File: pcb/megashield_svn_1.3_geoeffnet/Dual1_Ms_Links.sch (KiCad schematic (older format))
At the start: 7 parts, among them P18 Left

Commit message: Platine V1.3
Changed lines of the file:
@@
 LIBS:power
 LIBS:ardumower mega shield svn-cache
+LIBS:conn
 EELAYER 25 0
 EELAYER END
@@
 P 4895 3310
 AR Path="/553D8AD9/5542A35A/554BE910" Ref="#PWR0137"  Part="1"
-AR Path="/553D8AD9/554D3EE8/554BE910" Ref="#PWR0143"  Part="1"
-F 0 "#PWR0143" H 4895 3160 60  0001 C CNN
+AR Path="/553D8AD9/554D3EE8/554BE910" Ref="#PWR0145"  Part="1"
+F 0 "#PWR0145" H 4895 3160 60  0001 C CNN
 F 1 "+24V" H 4895 3450 60  0000 C CNN
 F 2 "" H 4895 3310 60  0000 C CNN
@@
 P 4895 4445
 AR Path="/553D8AD9/5542A35A/5542A3C5" Ref="#PWR0138"  Part="1"
-AR Path="/553D8AD9/554D3EE8/5542A3C5" Ref="#PWR0144"  Part="1"
-F 0 "#PWR0144" H 4895 4195 60  0001 C CNN
+AR Path="/553D8AD9/554D3EE8/5542A3C5" Ref="#PWR0146"  Part="1"
+F 0 "#PWR0146" H 4895 4195 60  0001 C CNN
 F 1 "GND" H 4895 4295 60  0000 C CNN
 F 2 "" H 4895 4445 60  0000 C CNN
@@
 P 4895 3580
 AR Path="/553D8AD9/5542A35A/5542A3D9" Ref="BY3"  Part="1"
-AR Path="/553D8AD9/554D3EE8/5542A3D9" Ref="BY7"  Part="1"
-F 0 "BY7" H 4895 3680 40  0000 C CNN
+AR Path="/553D8AD9/554D3EE8/5542A3D9" Ref="DBY7"  Part="1"
+F 0 "DBY7" H 4895 3680 40  0000 C CNN
 F 1 "BY 500/1000" H 4895 3480 40  0000 C CNN
 F 2 "ACS712:Diode_liegend_BY500_1000_RM10" H 4895 3580 60  0001 C CNN
@@
 P 4895 4140
 AR Path="/553D8AD9/5542A35A/5542A4FC" Ref="BY4"  Part="1"
-AR Path="/553D8AD9/554D3EE8/5542A4FC" Ref="BY8"  Part="1"
-F 0 "BY8" H 4895 4240 40  0000 C CNN
+AR Path="/553D8AD9/554D3EE8/5542A4FC" Ref="DBY8"  Part="1"
+F 0 "DBY8" H 4895 4240 40  0000 C CNN
 F 1 "BY 500/1000" H 4895 4040 40  0000 C CNN
 F 2 "ACS712:Diode_liegend_BY500_1000_RM10" H 4895 4140 60  0001 C CNN
@@
 P 3170 3310
 AR Path="/553D8AD9/5542A35A/5542A69A" Ref="#PWR0139"  Part="1"
-AR Path="/553D8AD9/554D3EE8/5542A69A" Ref="#PWR0145"  Part="1"
-F 0 "#PWR0145" H 3170 3160 60  0001 C CNN
+AR Path="/553D8AD9/554D3EE8/5542A69A" Ref="#PWR0147"  Part="1"
+F 0 "#PWR0147" H 3170 3160 60  0001 C CNN
 F 1 "+24V" H 3170 3450 60  0000 C CNN
 F 2 "" H 3170 3310 60  0000 C CNN
@@
 P 3170 4445
 AR Path="/553D8AD9/5542A35A/554BE919" Ref="#PWR0140"  Part="1"
-AR Path="/553D8AD9/554D3EE8/554BE919" Ref="#PWR0146"  Part="1"
-F 0 "#PWR0146" H 3170 4195 60  0001 C CNN
+AR Path="/553D8AD9/554D3EE8/554BE919" Ref="#PWR0148"  Part="1"
+F 0 "#PWR0148" H 3170 4195 60  0001 C CNN
 F 1 "GND" H 3170 4295 60  0000 C CNN
 F 2 "" H 3170 4445 60  0000 C CNN
@@
 P 3170 3580
 AR Path="/553D8AD9/5542A35A/554BE91B" Ref="BY1"  Part="1"
-AR Path="/553D8AD9/554D3EE8/554BE91B" Ref="BY5"  Part="1"
-F 0 "BY5" H 3170 3680 40  0000 C CNN
+AR Path="/553D8AD9/554D3EE8/554BE91B" Ref="DBY5"  Part="1"
+F 0 "DBY5" H 3170 3680 40  0000 C CNN
 F 1 "BY 500/1000" H 3170 3480 40  0000 C CNN
 F 2 "ACS712:Diode_liegend_BY500_1000_RM10" H 3170 3580 60  0001 C CNN
@@
 P 3170 4140
 AR Path="/553D8AD9/5542A35A/554BE91D" Ref="BY2"  Part="1"
-AR Path="/553D8AD9/554D3EE8/554BE91D" Ref="BY6"  Part="1"
-F 0 "BY6" H 3170 4240 40  0000 C CNN
+AR Path="/553D8AD9/554D3EE8/554BE91D" Ref="DBY6"  Part="1"
+F 0 "DBY6" H 3170 4240 40  0000 C CNN
 F 1 "BY 500/1000" H 3170 4040 40  0000 C CNN
 F 2 "ACS712:Diode_liegend_BY500_1000_RM10" H 3170 4140 60  0001 C CNN

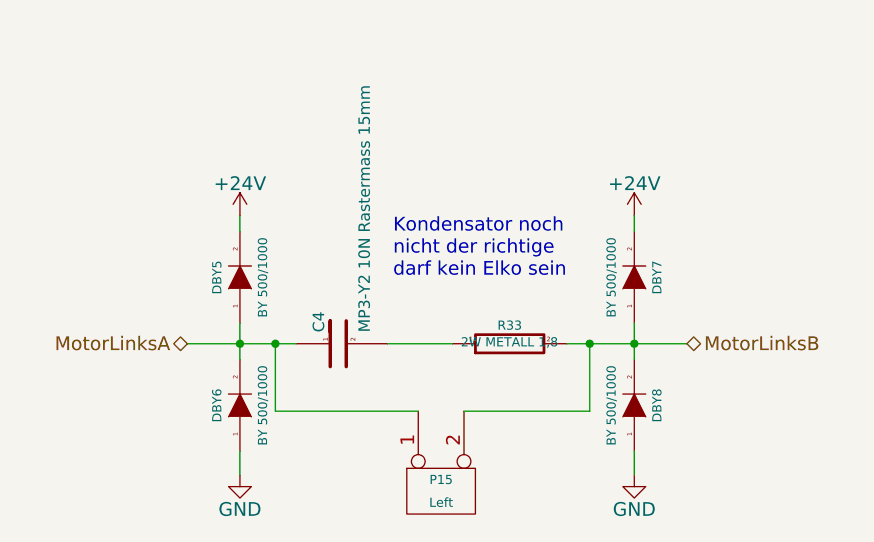
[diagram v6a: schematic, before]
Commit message: Platine V1.3
Einzelne Bauteile auf SMD angepasst
Belegung Anschlussstecker geändert +5V und GND
Anschlussstecker auf KK Stecker umgeändert
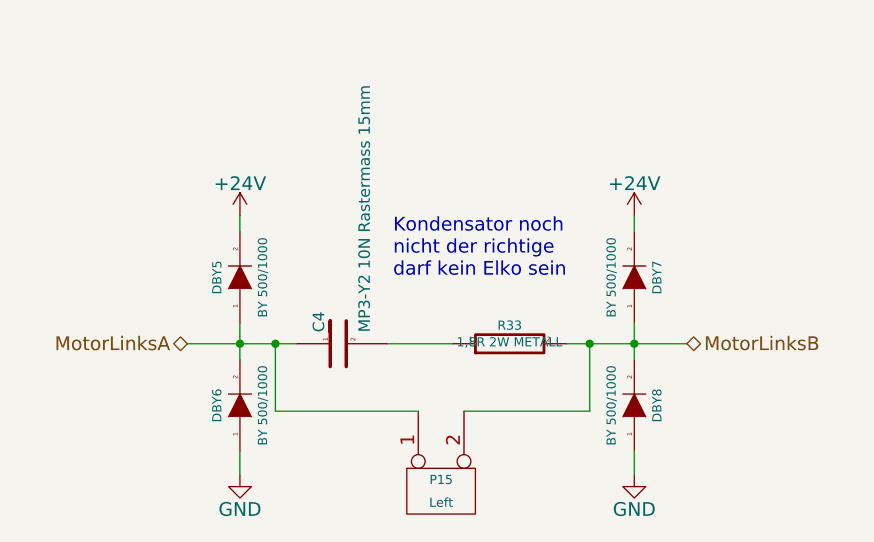
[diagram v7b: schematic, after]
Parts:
- BY1, BY2, BY3, BY4: footprint ACS712:Diode_liegend_BY500_1000_RM10 -> Diodes_ThroughHole:Diode_DO-201AD_Horizontal_RM15; Bauform (none) -> DO-201; Bestelllink (none) -> https://www.reichelt.de/BY-500-1000/3/index.html?&ACTION=3&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
- R33: value 2W METALL 1,8 -> 1,8R 2W METALL; footprint ACS712:Resistor_Horizontal_RM20mm -> Resistors_SMD:R_2512
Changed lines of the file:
@@
 $Descr A4 11693 8268
 encoding utf-8
-Sheet 15 27
+Sheet 15 25
 Title "Ardumower Shield - Motortreiber 1 - Links"
 Date ""
@@
 P 4895 3310
 AR Path="/553D8AD9/5542A35A/554BE910" Ref="#PWR0137"  Part="1"
-AR Path="/553D8AD9/554D3EE8/554BE910" Ref="#PWR0149"  Part="1"
-F 0 "#PWR0149" H 4895 3160 60  0001 C CNN
+AR Path="/553D8AD9/554D3EE8/554BE910" Ref="#PWR0159"  Part="1"
+F 0 "#PWR0159" H 4895 3160 60  0001 C CNN
 F 1 "+24V" H 4895 3450 60  0000 C CNN
 F 2 "" H 4895 3310 60  0000 C CNN
@@
 P 4895 4445
 AR Path="/553D8AD9/5542A35A/5542A3C5" Ref="#PWR0138"  Part="1"
-AR Path="/553D8AD9/554D3EE8/5542A3C5" Ref="#PWR0150"  Part="1"
-F 0 "#PWR0150" H 4895 4195 60  0001 C CNN
+AR Path="/553D8AD9/554D3EE8/5542A3C5" Ref="#PWR0160"  Part="1"
+F 0 "#PWR0160" H 4895 4195 60  0001 C CNN
 F 1 "GND" H 4895 4295 60  0000 C CNN
 F 2 "" H 4895 4445 60  0000 C CNN
@@
 F 0 "DBY7" H 4895 3680 40  0000 C CNN
 F 1 "BY 500/1000" H 4895 3480 40  0000 C CNN
-F 2 "ACS712:Diode_liegend_BY500_1000_RM10" H 4895 3580 60  0001 C CNN
+F 2 "Diodes_ThroughHole:Diode_DO-201AD_Horizontal_RM15" H 4895 3580 60  0001 C CNN
 F 3 "https://www.reichelt.de/BY-500-1000/3/index.html?&ACTION=3&LA=446&ARTICLE=6337&artnr=BY+500%2F1000&SEARCH=BY+500%2F1000" H 4895 3580 60  0001 C CNN
-F 4 "R: BY 500/1000" H 4895 3580 60  0001 C CNN "Bestellnummer"
-F 5 "Fast-Recovery-Gleichr.-Diode, DO201, 1000V, 5A" H 4895 3580 60  0001 C CNN "Technische Daten"
+F 4 "Fast-Recovery-Gleichr.-Diode, DO201, 1000V, 5A" H 4895 3580 60  0001 C CNN "Technische Daten"
+F 5 "R: BY 500/1000" H 4895 3580 60  0001 C CNN "Bestellnummer"
+F 6 "DO-201" H 4895 3580 60  0001 C CNN "Bauform"
+F 7 "https://www.reichelt.de/BY-500-1000/3/index.html?&ACTION=3&LA=446&ARTICLE=6337&artnr=BY+500%2F1000&SEARCH=BY+500%2F1000" H 4895 3580 60  0001 C CNN "Bestelllink"
 	1    4895 3580
 	0    1    -1   0
@@
 F 0 "DBY8" H 4895 4240 40  0000 C CNN
 F 1 "BY 500/1000" H 4895 4040 40  0000 C CNN
-F 2 "ACS712:Diode_liegend_BY500_1000_RM10" H 4895 4140 60  0001 C CNN
+F 2 "Diodes_ThroughHole:Diode_DO-201AD_Horizontal_RM15" H 4895 4140 60  0001 C CNN
 F 3 "https://www.reichelt.de/BY-500-1000/3/index.html?&ACTION=3&LA=446&ARTICLE=6337&artnr=BY+500%2F1000&SEARCH=BY+500%2F1000" H 4895 4140 60  0001 C CNN
-F 4 "R: BY 500/1000" H 4895 4140 60  0001 C CNN "Bestellnummer"
-F 5 "Fast-Recovery-Gleichr.-Diode, DO201, 1000V, 5A" H 4895 4140 60  0001 C CNN "Technische Daten"
+F 4 "Fast-Recovery-Gleichr.-Diode, DO201, 1000V, 5A" H 4895 4140 60  0001 C CNN "Technische Daten"
+F 5 "R: BY 500/1000" H 4895 4140 60  0001 C CNN "Bestellnummer"
+F 6 "DO-201" H 4895 4140 60  0001 C CNN "Bauform"
+F 7 "https://www.reichelt.de/BY-500-1000/3/index.html?&ACTION=3&LA=446&ARTICLE=6337&artnr=BY+500%2F1000&SEARCH=BY+500%2F1000" H 4895 4140 60  0001 C CNN "Bestelllink"
 	1    4895 4140
 	0    1    -1   0
@@
 P 3170 3310
 AR Path="/553D8AD9/5542A35A/5542A69A" Ref="#PWR0139"  Part="1"
-AR Path="/553D8AD9/554D3EE8/5542A69A" Ref="#PWR0151"  Part="1"
-F 0 "#PWR0151" H 3170 3160 60  0001 C CNN
+AR Path="/553D8AD9/554D3EE8/5542A69A" Ref="#PWR0161"  Part="1"
+F 0 "#PWR0161" H 3170 3160 60  0001 C CNN
 F 1 "+24V" H 3170 3450 60  0000 C CNN
 F 2 "" H 3170 3310 60  0000 C CNN
@@
 P 3170 4445
 AR Path="/553D8AD9/5542A35A/554BE919" Ref="#PWR0140"  Part="1"
-AR Path="/553D8AD9/554D3EE8/554BE919" Ref="#PWR0152"  Part="1"
-F 0 "#PWR0152" H 3170 4195 60  0001 C CNN
+AR Path="/553D8AD9/554D3EE8/554BE919" Ref="#PWR0162"  Part="1"
+F 0 "#PWR0162" H 3170 4195 60  0001 C CNN
 F 1 "GND" H 3170 4295 60  0000 C CNN
 F 2 "" H 3170 4445 60  0000 C CNN
@@
 F 0 "DBY5" H 3170 3680 40  0000 C CNN
 F 1 "BY 500/1000" H 3170 3480 40  0000 C CNN
-F 2 "ACS712:Diode_liegend_BY500_1000_RM10" H 3170 3580 60  0001 C CNN
+F 2 "Diodes_ThroughHole:Diode_DO-201AD_Horizontal_RM15" H 3170 3580 60  0001 C CNN
 F 3 "https://www.reichelt.de/BY-500-1000/3/index.html?&ACTION=3&LA=446&ARTICLE=6337&artnr=BY+500%2F1000&SEARCH=BY+500%2F1000" H 3170 3580 60  0001 C CNN
-F 4 "R: BY 500/1000" H 3170 3580 60  0001 C CNN "Bestellnummer"
-F 5 "Fast-Recovery-Gleichr.-Diode, DO201, 1000V, 5A" H 3170 3580 60  0001 C CNN "Technische Daten"
+F 4 "Fast-Recovery-Gleichr.-Diode, DO201, 1000V, 5A" H 3170 3580 60  0001 C CNN "Technische Daten"
+F 5 "R: BY 500/1000" H 3170 3580 60  0001 C CNN "Bestellnummer"
+F 6 "DO-201" H 3170 3580 60  0001 C CNN "Bauform"
+F 7 "https://www.reichelt.de/BY-500-1000/3/index.html?&ACTION=3&LA=446&ARTICLE=6337&artnr=BY+500%2F1000&SEARCH=BY+500%2F1000" H 3170 3580 60  0001 C CNN "Bestelllink"
 	1    3170 3580
 	0    -1   -1   0
@@
 F 0 "DBY6" H 3170 4240 40  0000 C CNN
 F 1 "BY 500/1000" H 3170 4040 40  0000 C CNN
-F 2 "ACS712:Diode_liegend_BY500_1000_RM10" H 3170 4140 60  0001 C CNN
+F 2 "Diodes_ThroughHole:Diode_DO-201AD_Horizontal_RM15" H 3170 4140 60  0001 C CNN
 F 3 "https://www.reichelt.de/BY-500-1000/3/index.html?&ACTION=3&LA=446&ARTICLE=6337&artnr=BY+500%2F1000&SEARCH=BY+500%2F1000" H 3170 4140 60  0001 C CNN
-F 4 "R: BY 500/1000" H 3170 4140 60  0001 C CNN "Bestellnummer"
-F 5 "Fast-Recovery-Gleichr.-Diode, DO201, 1000V, 5A" H 3170 4140 60  0001 C CNN "Technische Daten"
+F 4 "Fast-Recovery-Gleichr.-Diode, DO201, 1000V, 5A" H 3170 4140 60  0001 C CNN "Technische Daten"
+F 5 "R: BY 500/1000" H 3170 4140 60  0001 C CNN "Bestellnummer"
+F 6 "DO-201" H 3170 4140 60  0001 C CNN "Bauform"
+F 7 "https://www.reichelt.de/BY-500-1000/3/index.html?&ACTION=3&LA=446&ARTICLE=6337&artnr=BY+500%2F1000&SEARCH=BY+500%2F1000" H 3170 4140 60  0001 C CNN "Bestelllink"
 	1    3170 4140
 	0    -1   -1   0
@@
 AR Path="/553D8AD9/554D3EE8/554BE921" Ref="R33"  Part="1"
 F 0 "R33" V 4430 3870 40  0000 C CNN
-F 1 "2W METALL 1,8" V 4357 3871 40  0000 C CNN
-F 2 "ACS712:Resistor_Horizontal_RM20mm" V 4280 3870 30  0001 C CNN
+F 1 "1,8R 2W METALL" V 4357 3871 40  0000 C CNN
+F 2 "Resistors_SMD:R_2512" V 4280 3870 30  0001 C CNN
 F 3 "https://www.reichelt.de/2W-METALL-1-8/3/index.html?&ACTION=3&LA=446&ARTICLE=2309&artnr=2W+METALL+1%2C8&SEARCH=2W+METALL+1%2C8" H 4350 3870 30  0001 C CNN
 F 4 "R: 2W METALL 1,8" H 4350 3870 60  0001 C CNN "Bestellnummer"
